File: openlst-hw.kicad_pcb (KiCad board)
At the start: 4 copper layers, 50 x 28.8 mm, 69 parts, among them J3 Conn_02x10_Odd_Even, J6 ANT, U2 CC1110, U4 ASFL1-27.000MHZ, U5 MIC803, U6 PE4250, U7 RFFM6406, U8 SF2446E

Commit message: changed solder mask values in board setup
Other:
- rule pad_to_mask_clearance: 0.0381 -> 0
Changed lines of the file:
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@@
       (dielectric_constraints no)
     )
-    (pad_to_mask_clearance 0.0381)
-    (solder_mask_min_width 0.1016)
+    (pad_to_mask_clearance 0)
     (aux_axis_origin 137.3 115.4)
     (pcbplotparams

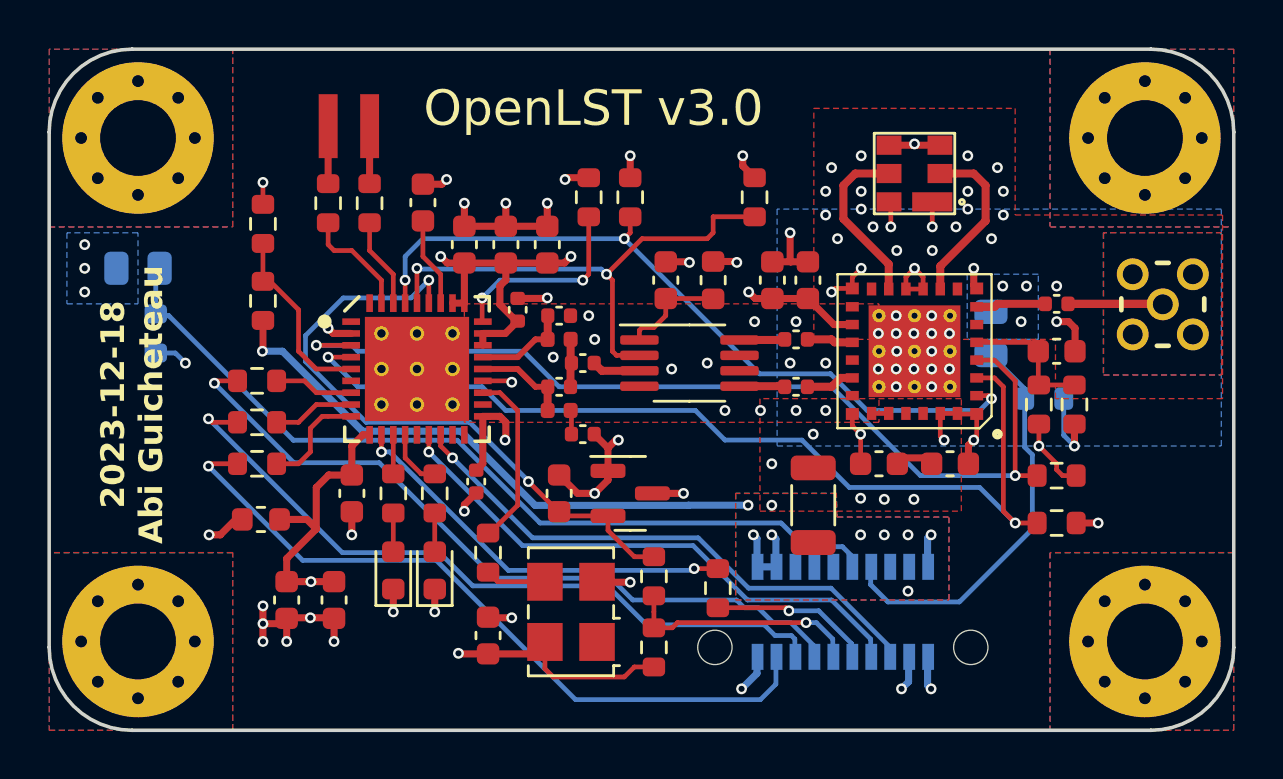
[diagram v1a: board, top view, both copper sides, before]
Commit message: added jlc order num
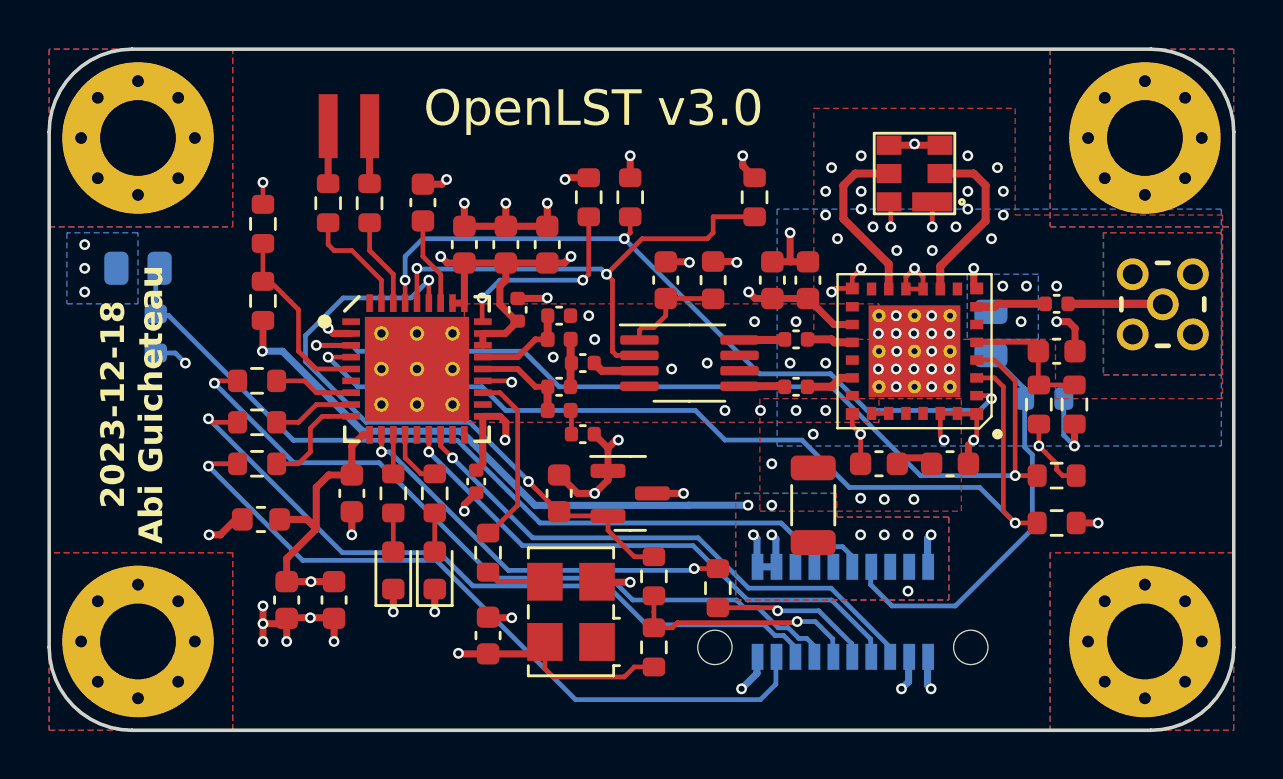
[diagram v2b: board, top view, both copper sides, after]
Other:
- board text added: "JLCJLCJLCJLC"
